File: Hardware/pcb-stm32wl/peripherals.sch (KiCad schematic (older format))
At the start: 29 parts, among them J1 Debug, J3 Grove_I2C, Q2 2SC4213, SW1 SW_Push, U5 MX25R1635, U6 LIS2DH12, U7 SHTC3, U8 ATECC608A-TNGLORAU

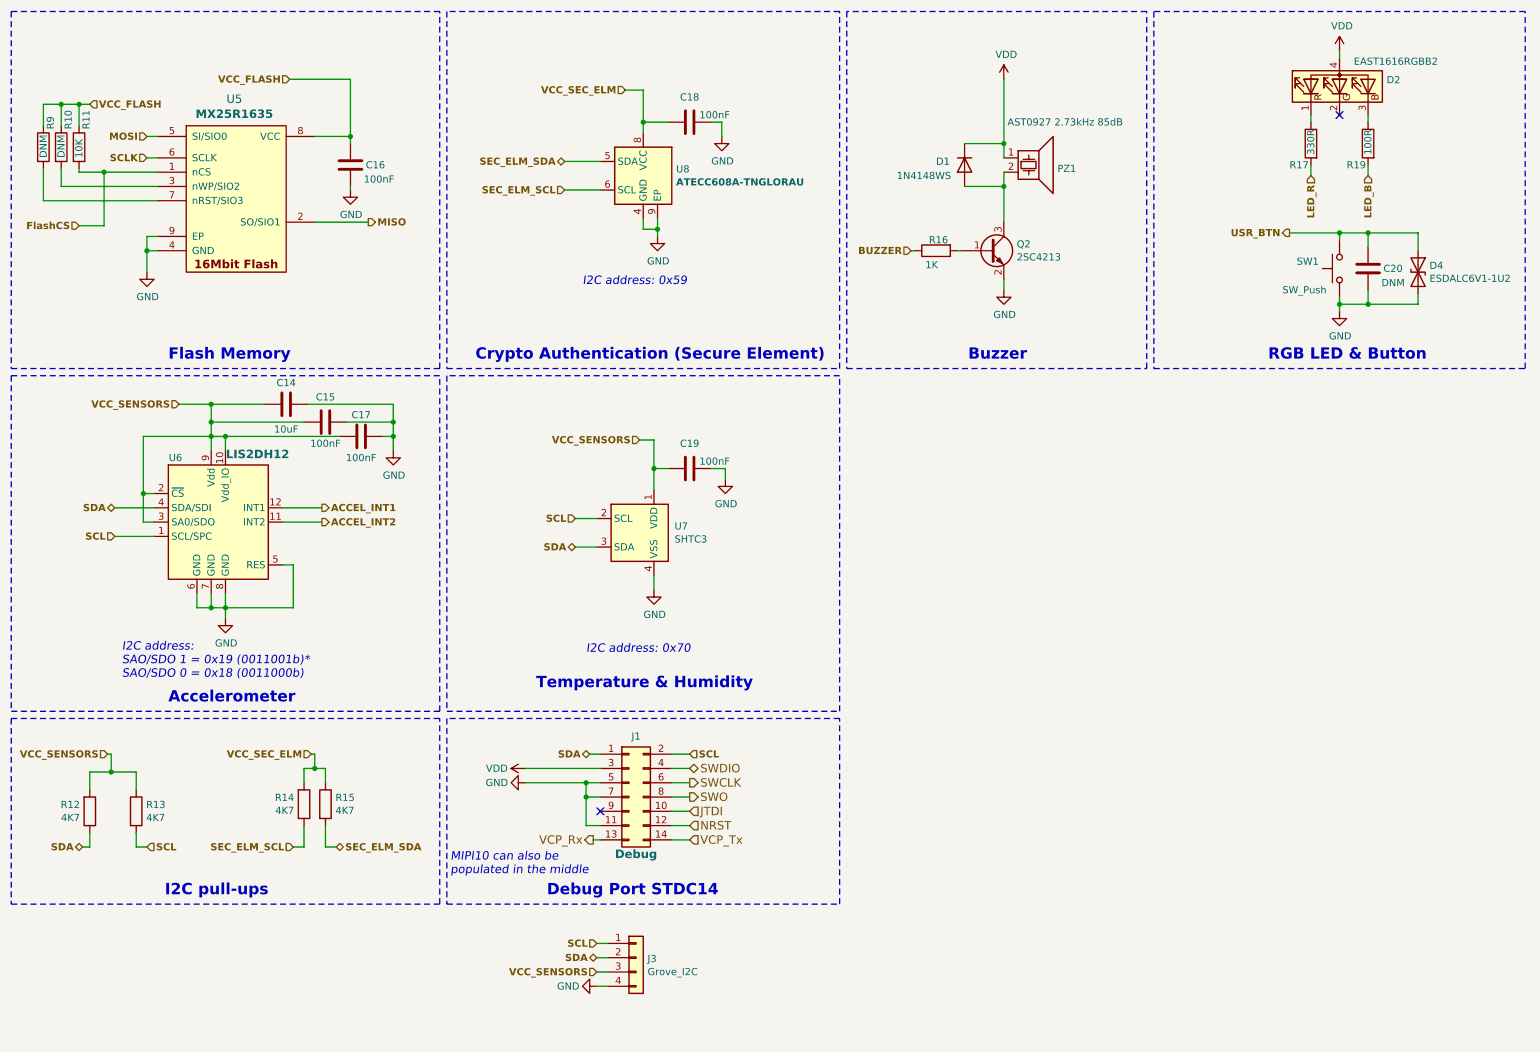
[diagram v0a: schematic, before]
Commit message: pcb,sch: Add V0.2 HW design with external battery holder
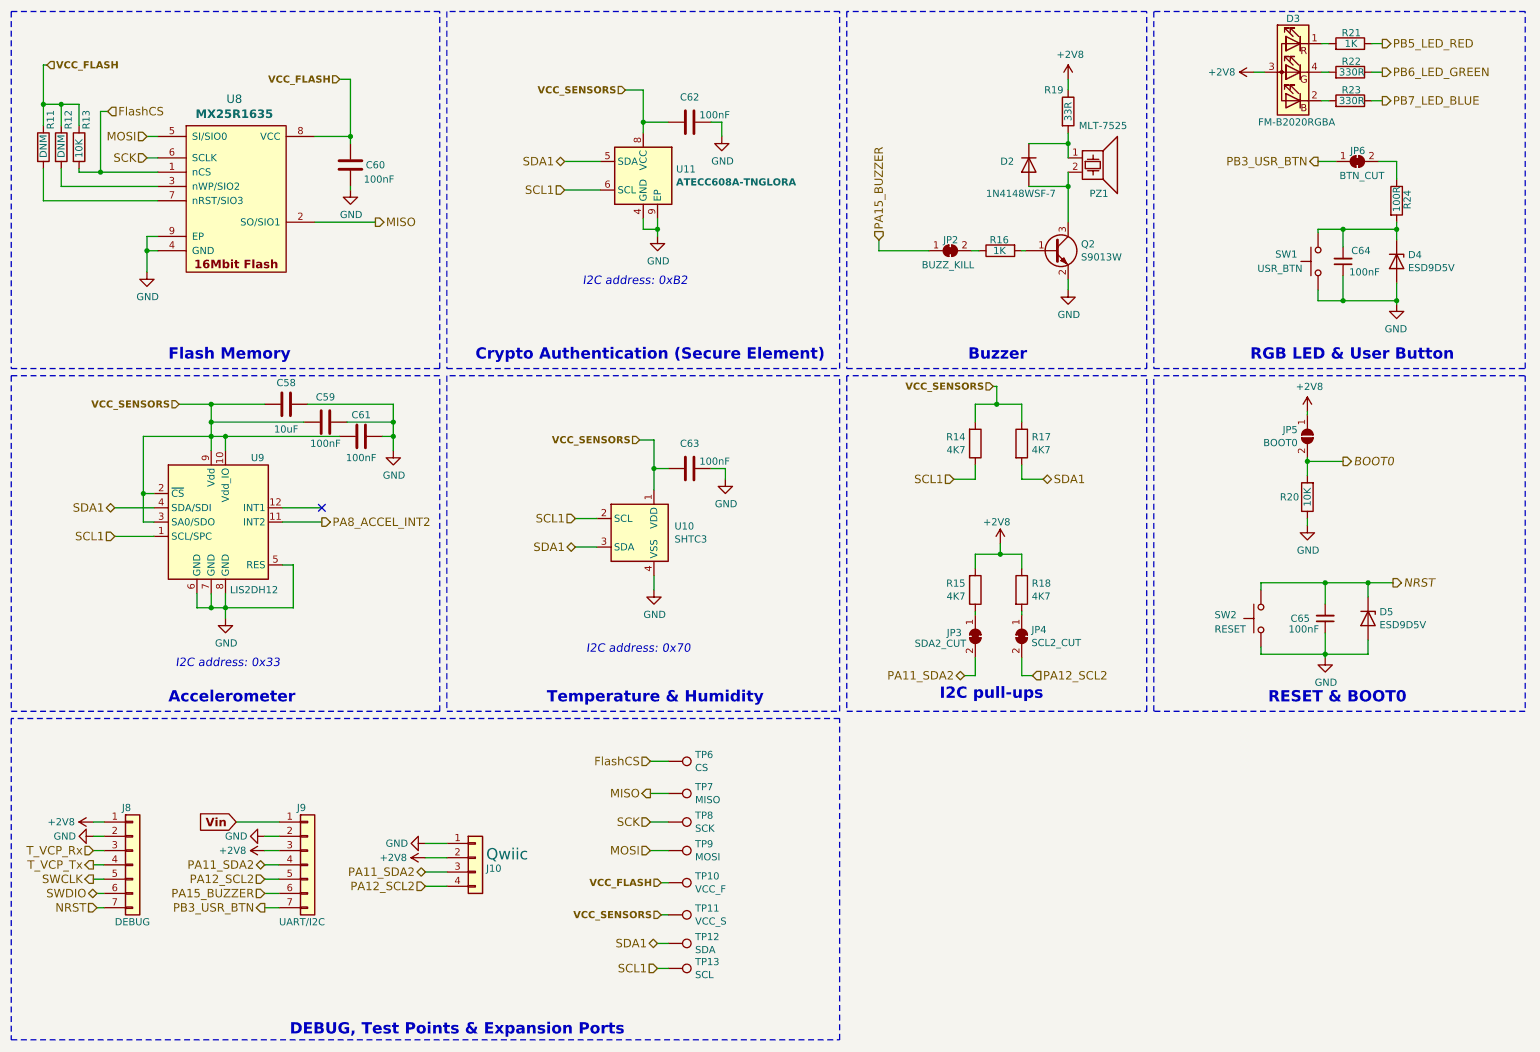
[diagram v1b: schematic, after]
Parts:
- removed C20: DNM, Capacitor_SMD:C_0402_1005Metric, symbol Device:C
- removed D2: EAST1616RGBB2, node-lib-v1:LED_RGB_0606, symbol Device:LED_RGBA
- removed D4: ESDALC6V1-1U2, Diode_SMD:D_0201_0603Metric, symbol Device:D_TVS
- removed J1: Debug, node-lib-v1:PinHeader_2x07_P1.27mm_Vertical_SMD, symbol Connector_Generic:Conn_02x07_Odd_Even
- removed J3: Grove_I2C, Connector:NS-Tech_Grove_1x04_P2mm_Vertical, symbol Connector_Generic:Conn_01x04
- removed R14: 4K7, Resistor_SMD:R_0402_1005Metric, symbol Device:R
- removed R17: 330R, Resistor_SMD:R_0402_1005Metric, symbol Device:R
- removed U6: LIS2DH12, Package_LGA:LGA-12_2x2mm_P0.5mm, symbol node-lib-v1:LIS2DH12
- added C64, C65: 100nF, Capacitor_SMD:C_0402_1005Metric, symbol Device:C_Small
- added D3: FM-B2020RGBA, LED_SMD:LED_Cree-PLCC4_2x2mm_CW, symbol node-lib-v1:FM-B2020RGBA
- added D4, D5: ESD9D5V, Diode_SMD:D_SOD-923, symbol Device:D_Zener
- added J10: Qwiic, Connector_JST:JST_SH_BM04B-SRSS-TB_1x04-1MP_P1.00mm_Vertical, symbol Connector_Generic:Conn_01x04
- added J8: DEBUG, Connector_PinSocket_2.54mm:PinSocket_1x07_P2.54mm_Vertical, symbol Connector_Generic:Conn_01x07
- added J9: UART/I2C, Connector_PinSocket_2.54mm:PinSocket_1x07_P2.54mm_Vertical, symbol Connector_Generic:Conn_01x07
- added JP2: BUZZ_KILL, Jumper:SolderJumper-2_P1.3mm_Bridged2Bar_RoundedPad1.0x1.5mm, symbol Jumper:SolderJumper_2_Bridged
- added JP3: SDA2_CUT, Jumper:SolderJumper-2_P1.3mm_Bridged2Bar_RoundedPad1.0x1.5mm, symbol Jumper:SolderJumper_2_Bridged
- added JP4: SCL2_CUT, Jumper:SolderJumper-2_P1.3mm_Bridged2Bar_RoundedPad1.0x1.5mm, symbol Jumper:SolderJumper_2_Bridged
- added JP5: BOOT0, Connector_PinHeader_1.27mm:PinHeader_1x02_P1.27mm_Vertical, symbol Jumper:SolderJumper_2_Open
- added JP6: BTN_CUT, Jumper:SolderJumper-2_P1.3mm_Bridged2Bar_RoundedPad1.0x1.5mm, symbol Jumper:SolderJumper_2_Bridged
- added R18: 4K7, Resistor_SMD:R_0402_1005Metric, symbol Device:R
- added R20: 10K, Inductor_SMD:L_0402_1005Metric, symbol Device:R
- added R21: 1K, Resistor_SMD:R_0402_1005Metric, symbol Device:R
- added R22, R23: 330R, Resistor_SMD:R_0402_1005Metric, symbol Device:R
- added R24: 100R, Resistor_SMD:R_0402_1005Metric, symbol Device:R
- added SW2: RESET, node-lib-v1:SW_SPST_SKSHABE010, symbol Switch:SW_Push
- added TP10: VCC_F, TestPoint:TestPoint_Pad_D1.5mm, symbol Connector:TestPoint
- added TP11: VCC_S, TestPoint:TestPoint_Pad_D1.5mm, symbol Connector:TestPoint
- added TP12: SDA, TestPoint:TestPoint_Pad_D1.5mm, symbol Connector:TestPoint
- added TP13: SCL, TestPoint:TestPoint_Pad_D1.5mm, symbol Connector:TestPoint
- added TP6: CS, TestPoint:TestPoint_Pad_D1.5mm, symbol Connector:TestPoint
- added TP7: MISO, TestPoint:TestPoint_Pad_D1.5mm, symbol Connector:TestPoint
- added TP8: SCK, TestPoint:TestPoint_Pad_D1.5mm, symbol Connector:TestPoint
- added TP9: MOSI, TestPoint:TestPoint_Pad_D1.5mm, symbol Connector:TestPoint
- added U9: LIS2DH12, Package_LGA:LGA-12_2x2mm_P0.5mm, symbol node-lib-v1:LIS2DH12
- C58: renamed from C14; ALT_MPN (none) -> C1608X5R0J106K080AB; MPN C1608X5R0J106K080AB -> JMK107ABJ106KA-T; URL (none) -> https://lcsc.com/product-detail/Others_Taiyo-Yuden_JMK107AB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
- C59: renamed from C15; URL (none) -> https://lcsc.com/product-detail/Multilayer-Ceramic-Capacito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
- C60: renamed from C16; URL (none) -> https://lcsc.com/product-detail/Multilayer-Ceramic-Capacito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
- C61: renamed from C17; URL (none) -> https://lcsc.com/product-detail/Multilayer-Ceramic-Capacito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
- C62: renamed from C18; URL (none) -> https://lcsc.com/product-detail/Multilayer-Ceramic-Capacito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
- C63: renamed from C19; URL (none) -> https://lcsc.com/product-detail/Multilayer-Ceramic-Capacito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
- D2: renamed from D1; value 1N4148WS -> 1N4148WSF-7; footprint Diode_SMD:D_SOD-323 -> node-lib-v1:D_SOD-323F_custom; MPN 1N4148WS-7-F -> 1N4148WSF-7; URL (none) -> https://lcsc.com/product-detail/Switching-Diode_Diodes-Inco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
- PZ1: value AST0927 2.73kHz 85dB -> MLT-7525; footprint node-lib-v1:Buzzer_AST0927MW-3.6TRQ -> node-lib-v1:Buzzer_MLT-7525; MPN AST0927MW-3.6TRQ -> MLT-7525; URL (none) -> https://lcsc.com/product-detail/Buzzers_Jiangsu-Huaneng-Ele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
- Q2: value 2SC4213 -> S9013W; MPN 2SC4213BTE85LF -> S9013W; URL (none) -> https://lcsc.com/product-detail/Transistors-NPN-PNP_Changji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
- R13: renamed from R11; URL (none) -> https://lcsc.com/product-detail/Chip-Resistor-Surface-Mount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
- R14: renamed from R12; URL (none) -> https://lcsc.com/product-detail/Chip-Resistor-Surface-Mount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
- R15: URL (none) -> https://lcsc.com/product-detail/Chip-Resistor-Surface-Mount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
- R16: MPN RC0402FR-071KP -> RC0402FR-071KL; URL (none) -> https://lcsc.com/product-detail/Chip-Resistor-Surface-Mount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
- R17: renamed from R13; URL (none) -> https://lcsc.com/product-detail/Chip-Resistor-Surface-Mount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
- R19: value 100R -> 33R; MPN RC0402FR-07100RL -> AC0402JR-0733RL; URL (none) -> https://lcsc.com/product-detail/_AC0402JR-0733RL_C144713.ht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
- SW1: value SW_Push -> USR_BTN; footprint node-lib-v1:EVQ-P2R02W -> node-lib-v1:PushButton_KSC721GLFS; MPN EVQ-P2R02W -> KSC721GLFS; URL (none) -> https://lcsc.com/product-detail/Tactile-Switches_C-K-KSC721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
- U10: renamed from U7; URL (none) -> https://lcsc.com/product-detail/Temperature-Humidity-Sensor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
- U11: renamed from U8; value ATECC608A-TNGLORAU -> ATECC608A-TNGLORA; URL (none) -> https://www.microchip.com/wwwproducts/en/ATECC608A-TNGLORA
- U8: renamed from U5; URL (none) -> https://www.digikey.com/short/zwbqjc
- renumbered R9 to R11, R10 to R12
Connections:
- net SEC_ELM_SCL is gone; now on net SCL1: U11.6 (SCL)
- net USR_BTN is gone; now on net GND: SW1.2
- net VDD is gone; now on an unnamed net: D2.1 (K), PZ1.1
- net FlashCS: now also TP6.1
- net GND: now also C64.1, C65.1, D4.2 (A), D5.2 (A), J10.1 (Pin_1), J8.2 (Pin_2), J9.2 (Pin_2), R20.1, SW2.1, U9.5 (RES), U9.6 (GND), U9.7 (GND), U9.8 (GND); no longer SW1.1
- net MISO: now also TP7.1
- net MOSI: now also TP9.1
- net NRST: now also C65.2, D5.1 (K), J8.7 (Pin_7), SW2.2
- net SWCLK: now also J8.5 (Pin_5)
- net SWDIO: now also J8.6 (Pin_6)
- net VCC_FLASH: now also TP10.1
- net VCC_SENSORS: now also C62.2, U11.8 (VCC), TP11.1, U9.10 (Vdd_IO), U9.2 (~CS), U9.3 (SA0/SDO), U9.9 (Vdd)
- net +2V8: now reaches R19.1
- net +2V8: now also R15.2, D3.3 (BK), J10.2 (Pin_2), J8.1 (Pin_1), J9.3 (Pin_3), JP5.1 (A), R18.1
- net BUZZER: no longer names the net of R16.1
- net BUZZER: now also JP2.2 (B)
- net LED_B: no longer names the net of R19.2
- net SCL renamed SCL1
- net SCL1: now also R14.1, TP13.1, U9.1 (SCL/SPC); no longer R17.2
- net SCLK renamed SCK
- net SCK: now also TP8.1
- net SDA renamed SDA1
- net SDA1: now also R17.2, U11.5 (SDA), TP12.1, U9.4 (SDA/SDI); no longer R14.1
- removed net SEC_ELM_SDA: R15.2, U11.5 (SDA)
- removed net VCC_SEC_ELM: C62.2, R15.1, U11.8 (VCC)
- new net: C64.2, D4.1 (K), R24.2, SW1.1
- new net: JP6.2 (B), R24.1
- new net: JP3.1 (A), R15.1
- new net: JP4.1 (A), R18.2
- new net: D3.4 (A), R22.2
- new net: D3.1 (RK), R21.2
- new net: D3.2 (GK), R23.2
- new net BOOT0: JP5.2 (B), R20.2
- new net PA11_SDA2: J10.3 (Pin_3), J9.4 (Pin_4), JP3.2 (B)
- new net PA12_SCL2: J10.4 (Pin_4), J9.5 (Pin_5), JP4.2 (B)
- new net PA15_BUZZER: J9.6 (Pin_6), JP2.1 (A)
- new net PA8_ACCEL_INT2: U9.11 (INT2)
- new net PB3_USR_BTN: J9.7 (Pin_7), JP6.1 (A)
- new net PB5_LED_RED: R21.1
- new net PB6_LED_GREEN: R22.1
- new net PB7_LED_BLUE: R23.1
- new net T_VCP_Rx: J8.3 (Pin_3)
- new net T_VCP_Tx: J8.4 (Pin_4)
- new net Vin: J9.1 (Pin_1)
- no-connect marks 2 -> 1
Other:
- note added: "DEBUG, Test Points & Expansion Ports"
- note added: "I2C address: 0x33"
- note added: "I2C address: 0xB2"
- note added: "RESET & BOOT0"
- note added: "RGB LED & User Button"
- note removed: "Debug Port STDC14"
- note removed: "I2C address: 0x59"
- note removed: "I2C address:\nSAO/SDO 1 = 0x19 (0011001b)*\nSAO/SDO 0 = 0x18 (0011000b)"
- note removed: "MIPI10 can also be \npopulated in the middle"
- note removed: "RGB LED & Button"
- moved on the sheet: D2, PZ1, Q2, R14, R16, R17, SW1
